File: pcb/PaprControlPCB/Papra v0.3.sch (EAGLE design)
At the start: 32 parts, among them Q1 AO3400A (C20917), U1 LP2985-50DBVR (C74511), U2 ATTINYX04SOIC14

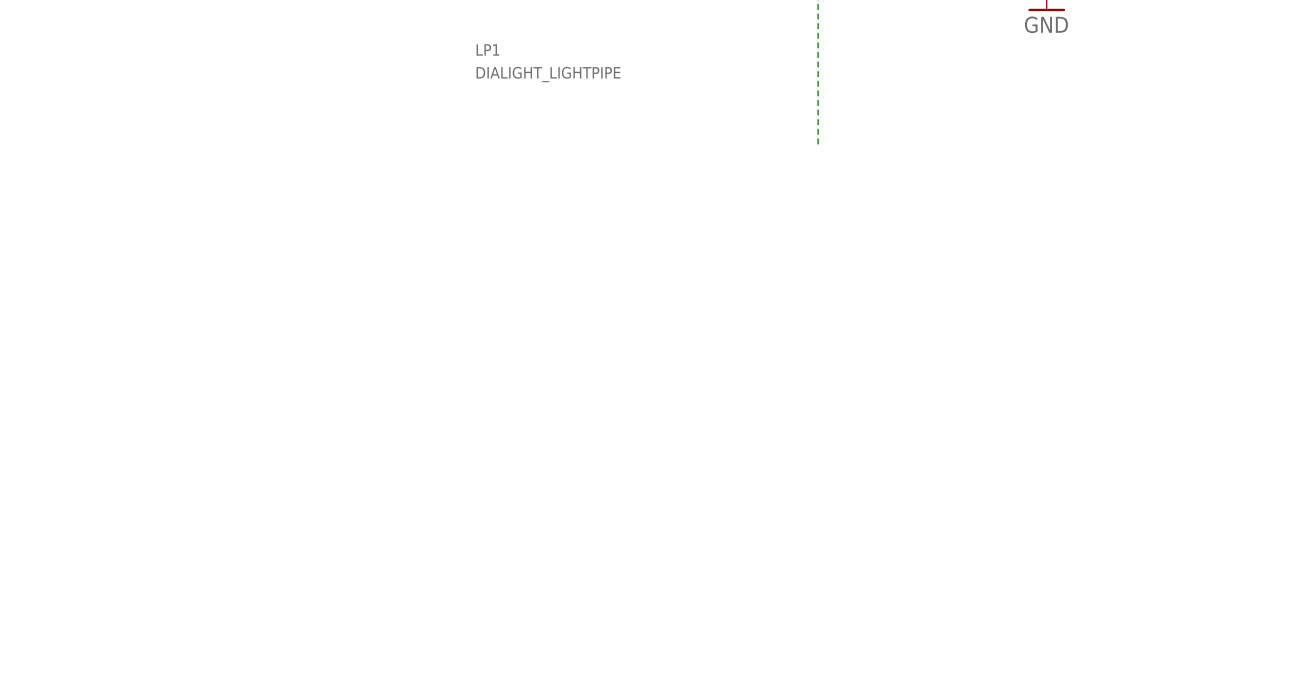
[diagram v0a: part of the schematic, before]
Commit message: Updating the boards for the 3rd build
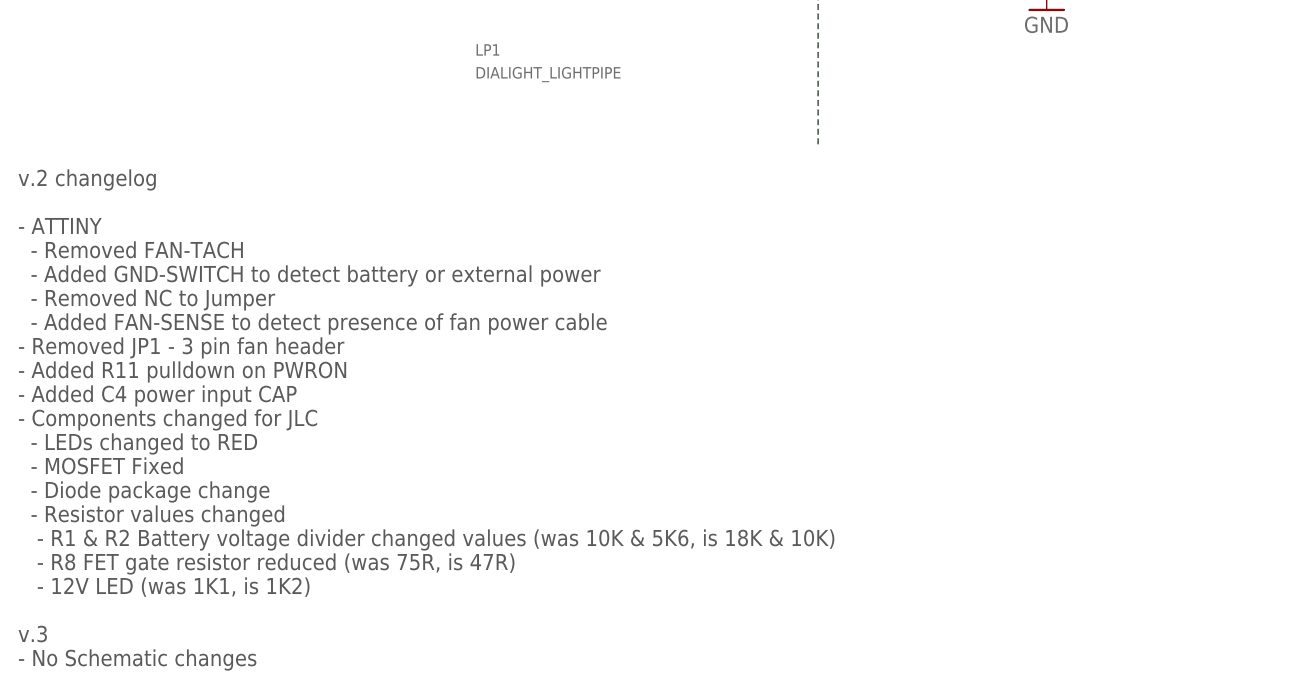
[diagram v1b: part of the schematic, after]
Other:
- note added: "v.2 changelog - ATTINY - Removed FAN-TACH - Added GND-SWITCH to detect battery or external power - Removed NC to Jumper - Added FAN-SENSE to detect presence of fan power cable - Removed JP1 - 3 pin fan header - Added R11 pulldown on PWRON - Added C4 power input CAP - Components changed for JLC - LEDs changed to RED - MOSFET Fixed - Diode package change - Resistor values changed - R1 & R2 Battery 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"
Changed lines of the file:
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@@
 <grid distance="0.1" unitdist="inch" unit="inch" style="lines" multiple="1" display="no" altdistance="0.01" altunitdist="inch" altunit="inch"/>
 <layers>
-<layer number="1" name="Top" color="4" fill="1" visible="yes" active="no"/>
-<layer number="2" name="Route2" color="16" fill="1" visible="yes" active="no"/>
-<layer number="3" name="Route3" color="17" fill="1" visible="yes" active="no"/>
-<layer number="4" name="Route4" color="18" fill="1" visible="yes" active="no"/>
-<layer number="5" name="Route5" color="19" fill="1" visible="yes" active="no"/>
-<layer number="6" name="Route6" color="25" fill="1" visible="yes" active="no"/>
-<layer number="7" name="Route7" color="26" fill="1" visible="yes" active="no"/>
-<layer number="8" name="Route8" color="27" fill="1" visible="yes" active="no"/>
-<layer number="9" name="Route9" color="28" fill="1" visible="yes" active="no"/>
-<layer number="10" name="Route10" color="29" fill="1" visible="yes" active="no"/>
-<layer number="11" name="Route11" color="30" fill="1" visible="yes" active="no"/>
-<layer number="12" name="Route12" color="20" fill="1" visible="yes" active="no"/>
-<layer number="13" name="Route13" color="21" fill="1" visible="yes" active="no"/>
-<layer number="14" name="Route14" color="22" fill="1" visible="yes" active="no"/>
-<layer number="15" name="Route15" color="23" fill="1" visible="yes" active="no"/>
-<layer number="16" name="Bottom" color="1" fill="1" visible="yes" active="no"/>
-<layer number="17" name="Pads" color="2" fill="1" visible="yes" active="no"/>
-<layer number="18" name="Vias" color="2" fill="1" visible="yes" active="no"/>
-<layer number="19" name="Unrouted" color="6" fill="1" visible="yes" active="no"/>
-<layer number="20" name="Dimension" color="24" fill="1" visible="yes" active="no"/>
-<layer number="21" name="tPlace" color="7" fill="1" visible="yes" active="no"/>
-<layer number="22" name="bPlace" color="7" fill="1" visible="yes" active="no"/>
-<layer number="23" name="tOrigins" color="15" fill="1" visible="yes" active="no"/>
-<layer number="24" name="bOrigins" color="15" fill="1" visible="yes" active="no"/>
-<layer number="25" name="tNames" color="7" fill="1" visible="yes" active="no"/>
-<layer number="26" name="bNames" color="7" fill="1" visible="yes" active="no"/>
-<layer number="27" name="tValues" color="7" fill="1" visible="yes" active="no"/>
-<layer number="28" name="bValues" color="7" fill="1" visible="yes" active="no"/>
+<layer number="1" name="Top" color="4" fill="1" visible="no" active="no"/>
+<layer number="2" name="Route2" color="16" fill="1" visible="no" active="no"/>
+<layer number="3" name="Route3" color="17" fill="1" visible="no" active="no"/>
+<layer number="4" name="Route4" color="18" fill="1" visible="no" active="no"/>
+<layer number="5" name="Route5" color="19" fill="1" visible="no" active="no"/>
+<layer number="6" name="Route6" color="25" fill="1" visible="no" active="no"/>
+<layer number="7" name="Route7" color="26" fill="1" visible="no" active="no"/>
+<layer number="8" name="Route8" color="27" fill="1" visible="no" active="no"/>
+<layer number="9" name="Route9" color="28" fill="1" visible="no" active="no"/>
+<layer number="10" name="Route10" color="29" fill="1" visible="no" active="no"/>
+<layer number="11" name="Route11" color="30" fill="1" visible="no" active="no"/>
+<layer number="12" name="Route12" color="20" fill="1" visible="no" active="no"/>
+<layer number="13" name="Route13" color="21" fill="1" visible="no" active="no"/>
+<layer number="14" name="Route14" color="22" fill="1" visible="no" active="no"/>
+<layer number="15" name="Route15" color="23" fill="1" visible="no" active="no"/>
+<layer number="16" name="Bottom" color="1" fill="1" visible="no" active="no"/>
+<layer number="17" name="Pads" color="2" fill="1" visible="no" active="no"/>
+<layer number="18" name="Vias" color="2" fill="1" visible="no" active="no"/>
+<layer number="19" name="Unrouted" color="6" fill="1" visible="no" active="no"/>
+<layer number="20" name="Dimension" color="24" fill="1" visible="no" active="no"/>
+<layer number="21" name="tPlace" color="7" fill="1" visible="no" active="no"/>
+<layer number="22" name="bPlace" color="7" fill="1" visible="no" active="no"/>
+<layer number="23" name="tOrigins" color="15" fill="1" visible="no" active="no"/>
+<layer number="24" name="bOrigins" color="15" fill="1" visible="no" active="no"/>
+<layer number="25" name="tNames" color="7" fill="1" visible="no" active="no"/>
+<layer number="26" name="bNames" color="7" fill="1" visible="no" active="no"/>
+<layer number="27" name="tValues" color="7" fill="1" visible="no" active="no"/>
+<layer number="28" name="bValues" color="7" fill="1" visible="no" active="no"/>
 <layer number="29" name="tStop" color="7" fill="3" visible="no" active="no"/>
 <layer number="30" name="bStop" color="7" fill="6" visible="no" active="no"/>
@@
 <layer number="35" name="tGlue" color="7" fill="4" visible="no" active="no"/>
 <layer number="36" name="bGlue" color="7" fill="5" visible="no" active="no"/>
-<layer number="37" name="tTest" color="7" fill="1" visible="yes" active="no"/>
-<layer number="38" name="bTest" color="7" fill="1" visible="yes" active="no"/>
+<layer number="37" name="tTest" color="7" fill="1" visible="no" active="no"/>
+<layer number="38" name="bTest" color="7" fill="1" visible="no" active="no"/>
 <layer number="39" name="tKeepout" color="4" fill="11" visible="no" active="no"/>
 <layer number="40" name="bKeepout" color="1" fill="11" visible="no" active="no"/>
@@
 <layer number="44" name="Drills" color="7" fill="1" visible="no" active="no"/>
 <layer number="45" name="Holes" color="7" fill="1" visible="no" active="no"/>
-<layer number="46" name="Milling" color="3" fill="1" visible="yes" active="no"/>
-<layer number="47" name="Measures" color="7" fill="1" visible="yes" active="no"/>
-<layer number="48" name="Document" color="7" fill="1" visible="yes" active="no"/>
-<layer number="49" name="Reference" color="7" fill="1" visible="yes" active="no"/>
-<layer number="50" name="dxf" color="3" fill="1" visible="yes" active="no"/>
-<layer number="51" name="tDocu" color="7" fill="1" visible="yes" active="no"/>
-<layer number="52" name="bDocu" color="7" fill="1" visible="yes" active="no"/>
-<layer number="53" name="tGND_GNDA" color="7" fill="9" visible="yes" active="no"/>
-<layer number="54" name="bGND_GNDA" color="1" fill="9" visible="yes" active="no"/>
-<layer number="56" name="wert" color="7" fill="1" visible="yes" active="no"/>
-<layer number="57" name="tCAD" color="7" fill="1" visible="yes" active="no"/>
-<layer number="59" name="tCarbon" color="7" fill="1" visible="yes" active="no"/>
-<layer number="60" name="bCarbon" color="7" fill="1" visible="yes" active="no"/>
+<layer number="46" name="Milling" color="3" fill="1" visible="no" active="no"/>
+<layer number="47" name="Measures" color="7" fill="1" visible="no" active="no"/>
+<layer number="48" name="Document" color="7" fill="1" visible="no" active="no"/>
+<layer number="49" name="Reference" color="7" fill="1" visible="no" active="no"/>
+<layer number="50" name="dxf" color="3" fill="1" visible="no" active="no"/>
+<layer number="51" name="tDocu" color="7" fill="1" visible="no" active="no"/>
+<layer number="52" name="bDocu" color="7" fill="1" visible="no" active="no"/>
+<layer number="53" name="tGND_GNDA" color="7" fill="9" visible="no" active="no"/>
+<layer number="54" name="bGND_GNDA" color="1" fill="9" visible="no" active="no"/>
+<layer number="56" name="wert" color="7" fill="1" visible="no" active="no"/>
+<layer number="57" name="tCAD" color="7" fill="1" visible="no" active="no"/>
+<layer number="59" name="tCarbon" color="7" fill="1" visible="no" active="no"/>
+<layer number="60" name="bCarbon" color="7" fill="1" visible="no" active="no"/>
 <layer number="88" name="SimResults" color="9" fill="1" visible="yes" active="yes"/>
 <layer number="89" name="SimProbes" color="9" fill="1" visible="yes" active="yes"/>
@@
 ALTERNATE: AP7380-50W5-7
 </text>
+<text x="0" y="-2.54" size="1.778" layer="97" font="vector" align="top-left">v.2 changelog
+- ATTINY
+  - Removed FAN-TACH
+  - Added GND-SWITCH to detect battery or external power
+  - Removed NC to Jumper
+  - Added FAN-SENSE to detect presence of fan power cable
+- Removed JP1 - 3 pin fan header
+- Added R11 pulldown on PWRON
+- Added C4 power input CAP
+- Components changed for JLC
+  - LEDs changed to RED
+  - MOSFET Fixed
+  - Diode package change
+  - Resistor values changed
+   - R1 &amp; R2 Battery voltage divider changed values (was 10K &amp; 5K6, is 18K &amp; 10K)
+   - R8 FET gate resistor reduced (was 75R, is 47R)
+   - 12V LED (was 1K1, is 1K2)
+v.3
+- No Schematic changes</text>
 </plain>
 <instances>
